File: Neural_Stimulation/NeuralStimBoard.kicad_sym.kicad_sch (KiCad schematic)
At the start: 52 parts, among them U1 CSI040

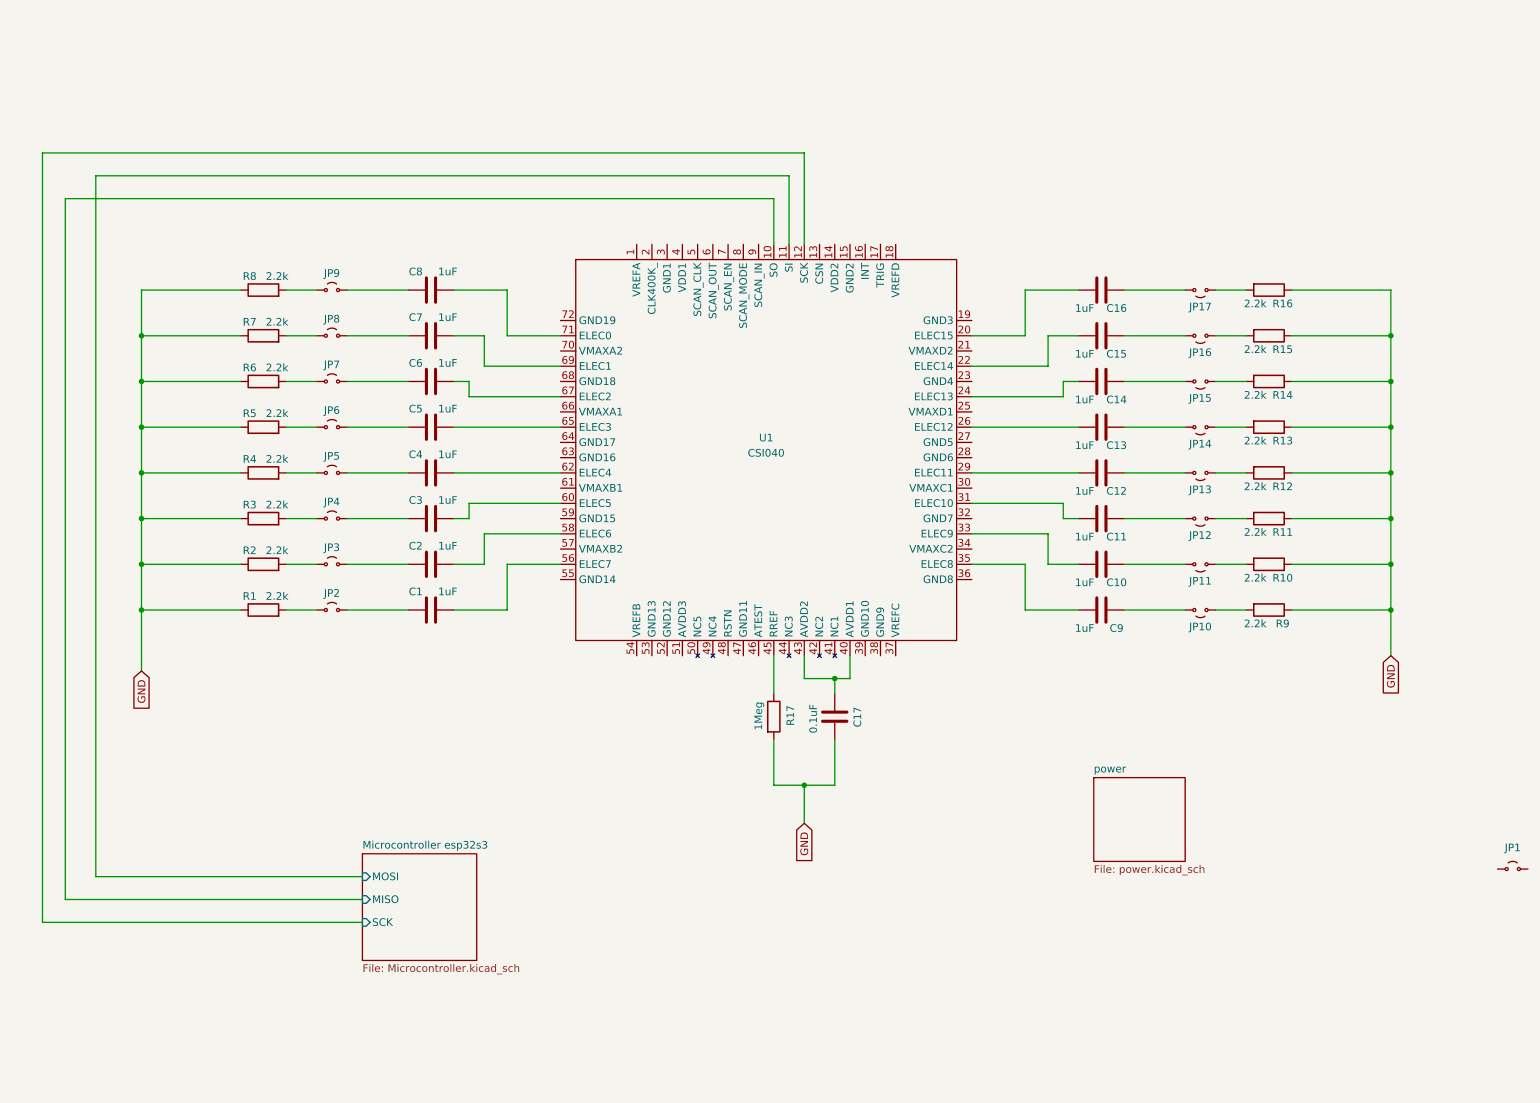
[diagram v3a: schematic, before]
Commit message: Added level shifters
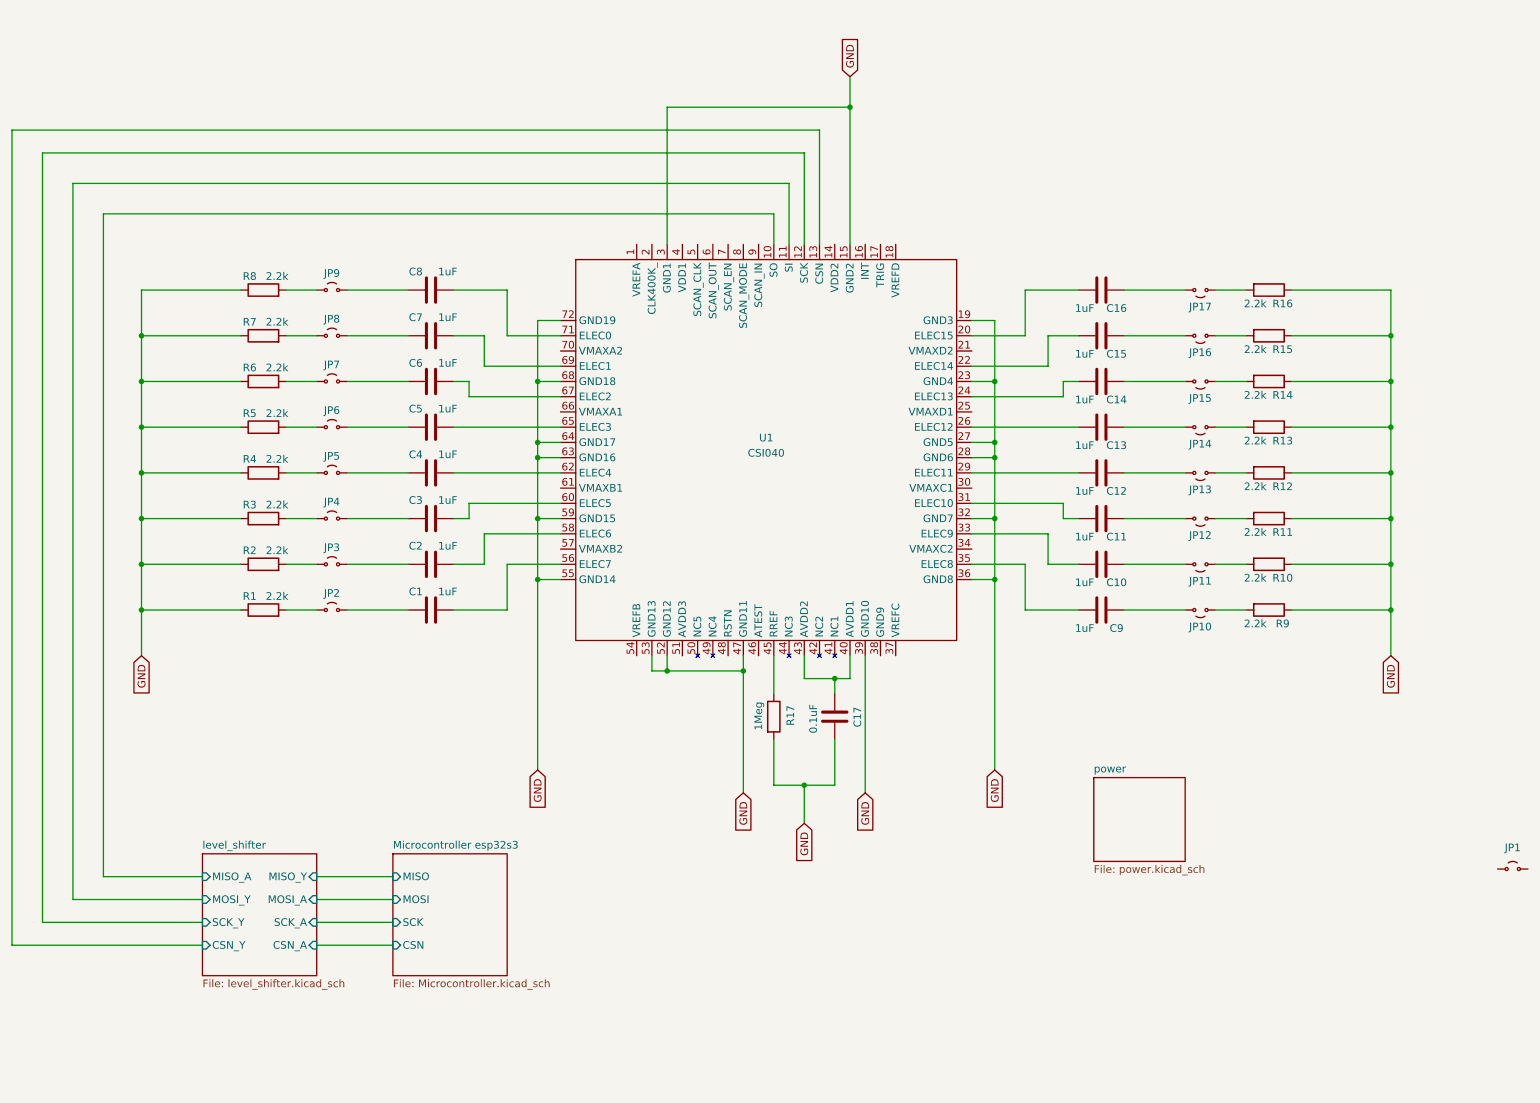
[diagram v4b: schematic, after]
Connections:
- net GND: now also U1.15 (GND2), U1.19 (GND3), U1.23 (GND4), U1.27 (GND5), U1.28 (GND6), U1.3 (GND1), U1.32 (GND7), U1.36 (GND8), U1.39 (GND10), U1.47 (GND11), U1.52 (GND12), U1.53 (GND13), U1.55 (GND14), U1.59 (GND15), U1.63 (GND16), U1.64 (GND17), U1.68 (GND18), U1.72 (GND19)
- net Microcontroller esp32s3/MISO: no longer U1.10 (SO)
- net Microcontroller esp32s3/MOSI: no longer U1.11 (SI)
- net Microcontroller esp32s3/SCK: no longer U1.12 (SCK)
- net level_shifter/CSN_Y: now reaches U1.13 (CSN)
- new net level_shifter/MISO_A: U1.10 (SO)
- new net level_shifter/MOSI_Y: U1.11 (SI)
- new net level_shifter/SCK_Y: U1.12 (SCK)
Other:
- added sheet level_shifter (level_shifter.kicad_sch)
- sheet Microcontroller esp32s3 ports: added CSN; removed none

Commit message: Added boost converter for generating VMAX
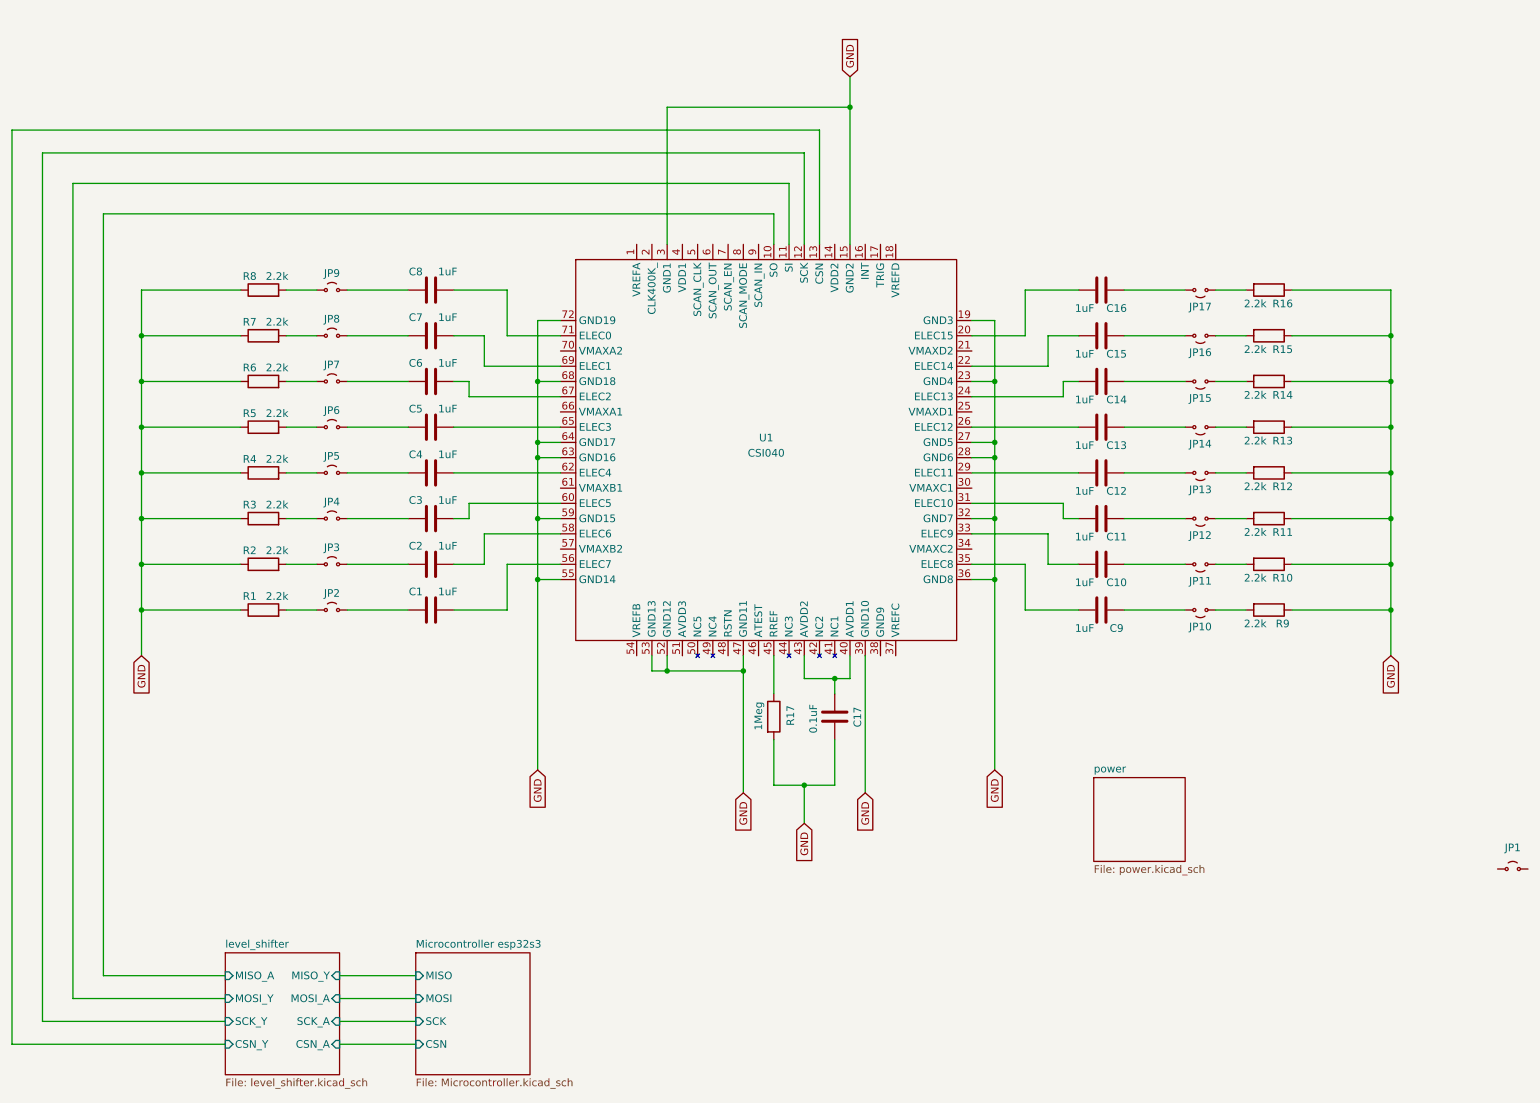
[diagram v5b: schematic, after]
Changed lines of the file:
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@@
 	(wire
 		(pts
-			(xy 31.75 158.75) (xy 53.34 158.75)
+			(xy 31.75 175.26) (xy 57.15 175.26)
 		)
 		(stroke
@@
 	(wire
 		(pts
-			(xy 36.83 154.94) (xy 36.83 44.45)
+			(xy 36.83 171.45) (xy 36.83 44.45)
 		)
 		(stroke
@@
 	(wire
 		(pts
-			(xy 53.34 162.56) (xy 26.67 162.56)
+			(xy 57.15 179.07) (xy 26.67 179.07)
 		)
 		(stroke
@@
 	(wire
 		(pts
-			(xy 26.67 34.29) (xy 26.67 162.56)
+			(xy 26.67 34.29) (xy 26.67 179.07)
 		)
 		(stroke
@@
 	(wire
 		(pts
-			(xy 72.39 166.37) (xy 85.09 166.37)
+			(xy 76.2 182.88) (xy 88.9 182.88)
 		)
 		(stroke
@@
 	(wire
 		(pts
-			(xy 72.39 154.94) (xy 85.09 154.94)
+			(xy 76.2 171.45) (xy 88.9 171.45)
 		)
 		(stroke
@@
 	(wire
 		(pts
-			(xy 21.59 166.37) (xy 21.59 30.48)
+			(xy 21.59 182.88) (xy 21.59 30.48)
 		)
 		(stroke
@@
 	(wire
 		(pts
-			(xy 36.83 154.94) (xy 53.34 154.94)
+			(xy 36.83 171.45) (xy 57.15 171.45)
 		)
 		(stroke
@@
 	(wire
 		(pts
-			(xy 72.39 158.75) (xy 85.09 158.75)
+			(xy 76.2 175.26) (xy 88.9 175.26)
 		)
 		(stroke
@@
 	(wire
 		(pts
-			(xy 72.39 162.56) (xy 85.09 162.56)
+			(xy 76.2 179.07) (xy 88.9 179.07)
 		)
 		(stroke
@@
 	(wire
 		(pts
-			(xy 31.75 158.75) (xy 31.75 39.37)
+			(xy 31.75 175.26) (xy 31.75 39.37)
 		)
 		(stroke
@@
 	(wire
 		(pts
-			(xy 21.59 166.37) (xy 53.34 166.37)
+			(xy 21.59 182.88) (xy 57.15 182.88)
 		)
 		(stroke
@@
 	)
 	(sheet
-		(at 85.09 151.13)
+		(at 88.9 167.64)
 		(size 19.05 20.32)
 		(fields_autoplaced yes)
@@
 		)
 		(property "Sheetname" "Microcontroller esp32s3"
-			(at 85.09 150.4184 0)
+			(at 88.9 166.9284 0)
 			(effects
 				(font
@@
 		)
 		(property "Sheetfile" "Microcontroller.kicad_sch"
-			(at 85.09 172.0346 0)
+			(at 88.9 188.5446 0)
 			(effects
 				(font
@@
 		)
 		(pin "MOSI" input
-			(at 85.09 158.75 180)
+			(at 88.9 175.26 180)
 			(effects
 				(font
@@
 		)
 		(pin "MISO" input
-			(at 85.09 154.94 180)
+			(at 88.9 171.45 180)
 			(effects
 				(font
@@
 		)
 		(pin "SCK" input
-			(at 85.09 162.56 180)
+			(at 88.9 179.07 180)
 			(effects
 				(font
@@
 		)
 		(pin "CSN" input
-			(at 85.09 166.37 180)
+			(at 88.9 182.88 180)
 			(effects
 				(font
@@
 	)
 	(sheet
-		(at 53.34 151.13)
+		(at 57.15 167.64)
 		(size 19.05 20.32)
 		(fields_autoplaced yes)
@@
 		)
 		(property "Sheetname" "level_shifter"
-			(at 53.34 150.4184 0)
+			(at 57.15 166.9284 0)
 			(effects
 				(font
@@
 		)
 		(property "Sheetfile" "level_shifter.kicad_sch"
-			(at 53.34 172.0346 0)
+			(at 57.15 188.5446 0)
 			(effects
 				(font
@@
 		)
 		(pin "MISO_Y" input
-			(at 72.39 154.94 0)
+			(at 76.2 171.45 0)
 			(effects
 				(font
@@
 		)
 		(pin "MISO_A" input
-			(at 53.34 154.94 180)
+			(at 57.15 171.45 180)
 			(effects
 				(font
@@
 		)
 		(pin "MOSI_Y" input
-			(at 53.34 158.75 180)
+			(at 57.15 175.26 180)
 			(effects
 				(font
@@
 		)
 		(pin "MOSI_A" input
-			(at 72.39 158.75 0)
+			(at 76.2 175.26 0)
 			(effects
 				(font
@@
 		)
 		(pin "CSN_A" input
-			(at 72.39 166.37 0)
+			(at 76.2 182.88 0)
 			(effects
 				(font
@@
 		)
 		(pin "SCK_A" input
-			(at 72.39 162.56 0)
+			(at 76.2 179.07 0)
 			(effects
 				(font
@@
 		)
 		(pin "SCK_Y" input
-			(at 53.34 162.56 180)
+			(at 57.15 179.07 180)
 			(effects
 				(font
@@
 		)
 		(pin "CSN_Y" input
-			(at 53.34 166.37 180)
+			(at 57.15 182.88 180)
 			(effects
 				(font

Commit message: Made VMAX connections to CSI040
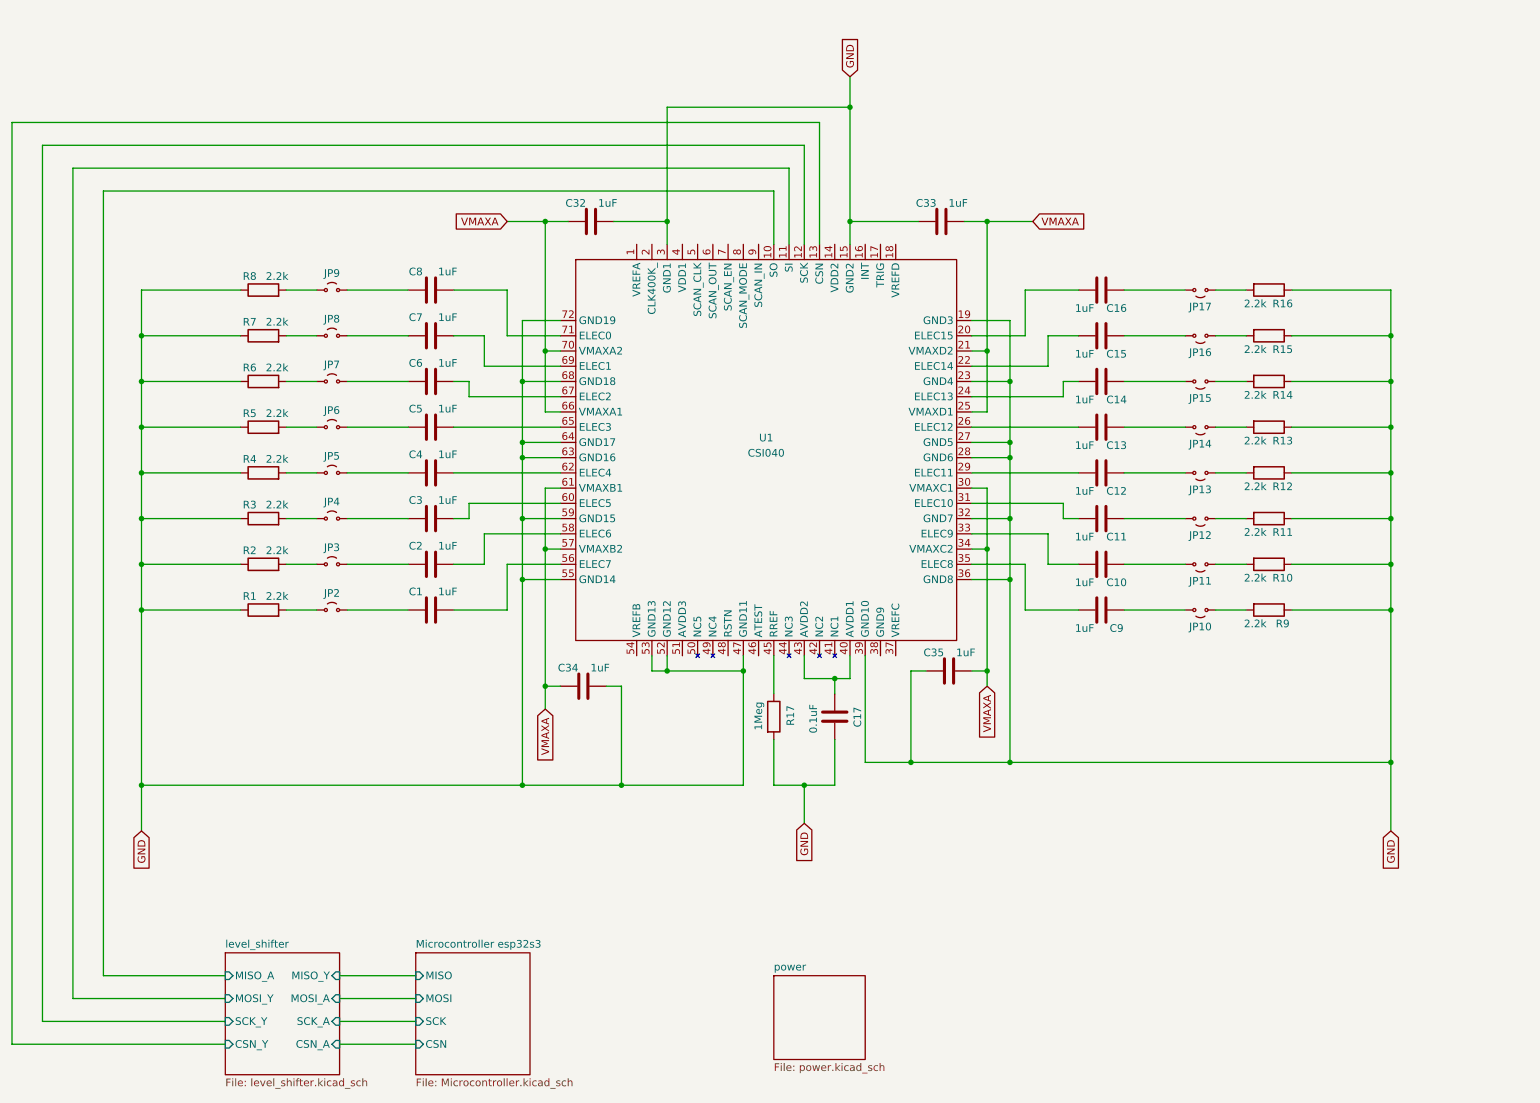
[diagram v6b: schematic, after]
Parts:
- removed JP1: Jumper_2_Small_Open, symbol Jumper:Jumper_2_Small_Open
- added C32, C33, C34, C35: 1uF, symbol Device:C
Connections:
- net GND: now also C32.2, C33.1, C34.2, C35.1
- net VMAXA: now reaches U1.21 (VMAXD2)
- net VMAXA: now also U1.25 (VMAXD1), U1.30 (VMAXC1), U1.34 (VMAXC2), U1.57 (VMAXB2), U1.61 (VMAXB1), U1.66 (VMAXA1), U1.70 (VMAXA2), C32.1, C33.2, C34.1, C35.2

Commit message: Added VREF Connections
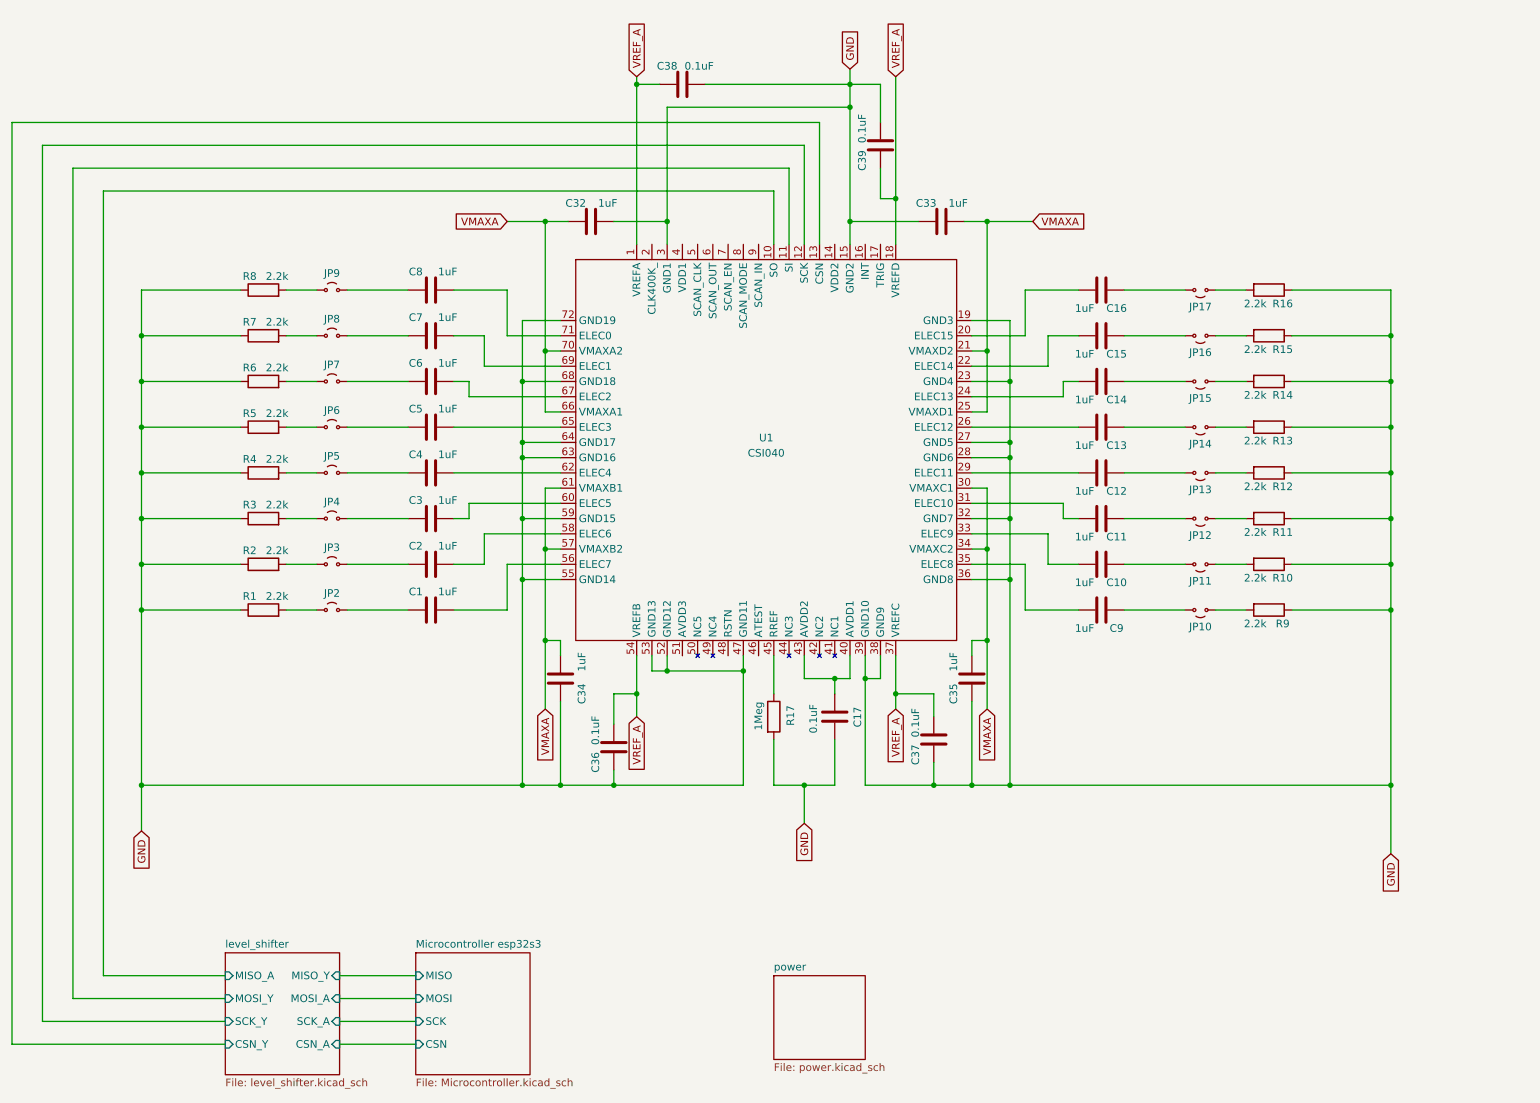
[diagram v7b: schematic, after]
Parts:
- added C36, C37, C38, C39: 0.1uF, symbol Device:C
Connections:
- net GND: now also C34.1, U1.38 (GND9), C36.1, C37.1, C38.2, C39.2; no longer C34.2
- net VMAXA: now also C34.2; no longer C34.1
- net VREF_A: now reaches U1.1 (VREFA)
- net VREF_A: now also U1.18 (VREFD), U1.37 (VREFC), U1.54 (VREFB), C36.2, C37.2, C38.1, C39.1
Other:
- moved on the sheet: C34, C35
